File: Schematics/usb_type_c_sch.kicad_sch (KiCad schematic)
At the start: 4 parts, among them J2 USB_C_Receptacle

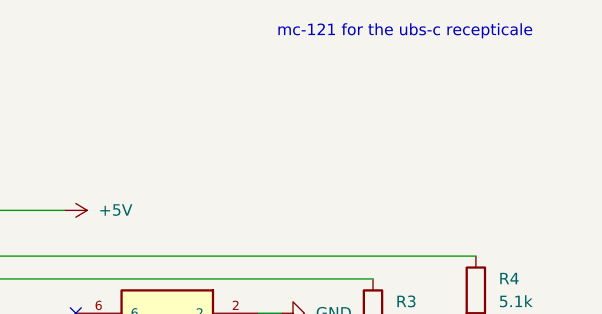
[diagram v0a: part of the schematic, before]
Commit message: finished sensor schematics, added datasheets organized files
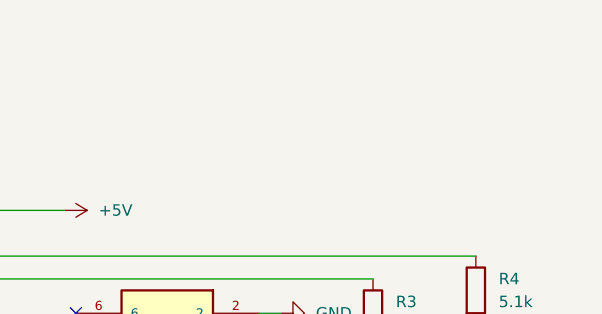
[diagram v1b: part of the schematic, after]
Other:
- note removed: "mc-121 for the ubs-c recepticale"
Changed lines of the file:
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@@
 	(generator_version "9.0")
 	(paper "A4")
-	(text "\n"
-		(exclude_from_sim no)
-		(at 157.226 37.338 0)
-		(effects
-			(font
-				(size 1.27 1.27)
-			)
-		)
-	)
-	(text "mc-121 for the ubs-c recepticale\n"
-		(exclude_from_sim no)
-		(at 178.816 37.338 0)
-		(effects
-			(font
-				(size 1.27 1.27)
-			)
-		)
-	)
 	(junction
 		(at 129.54 71.12)

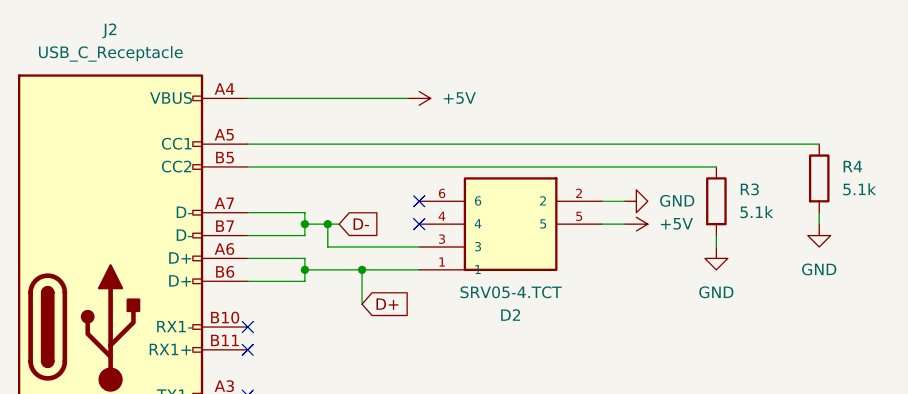
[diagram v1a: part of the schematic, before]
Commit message: added LCSC numbers and footprint values, need to connect schemeatic pins, then can start layout
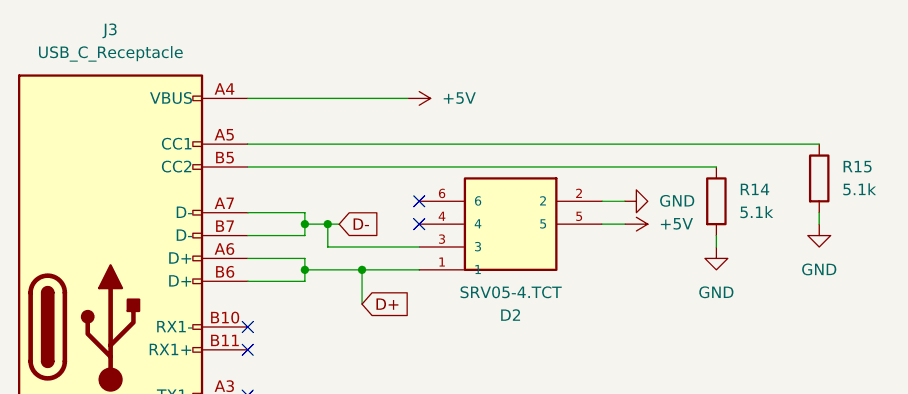
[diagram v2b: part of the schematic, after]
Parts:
- D2: footprint Library:SOT95P280X145-6N -> myFootprints:SOT95P280X145-6N; LCSC Part (none) -> C13612
- J3: renamed from J2; LCSC Part (none) -> C49566391
- R14: renamed from R3; LCSC Part (none) -> C27834
- R15: renamed from R4; LCSC Part (none) -> C27834
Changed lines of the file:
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@@
 		(dnp no)
 		(fields_autoplaced yes)
-		(property "Reference" "J2"
+		(property "Reference" "J3"
 			(at 107.95 49.53 0)
 			(effects
@@
 		)
 		(property "Description" "USB Full-Featured Type-C Receptacle connector"
+			(at 107.95 82.55 0)
+			(effects
+				(font
+					(size 1.27 1.27)
+				)
+				(hide yes)
+			)
+		)
+		(property "Sim.Device" ""
+			(at 107.95 82.55 0)
+			(effects
+				(font
+					(size 1.27 1.27)
+				)
+				(hide yes)
+			)
+		)
+		(property "Sim.Type" ""
+			(at 107.95 82.55 0)
+			(effects
+				(font
+					(size 1.27 1.27)
+				)
+				(hide yes)
+			)
+		)
+		(property "LCSC Part" "C49566391"
 			(at 107.95 82.55 0)
 			(effects
@@
 			(project "flightcomputer2"
 				(path "/6cb3dda3-5fe8-4715-b831-354360aa3199/105f27ec-5fab-44f4-a683-69b23a7486f0"
-					(reference "J2")
+					(reference "J3")
 					(unit 1)
 				)
@@
 			)
 		)
-		(property "Footprint" "Library:SOT95P280X145-6N"
+		(property "Footprint" "myFootprints:SOT95P280X145-6N"
 			(at 162.56 73.66 0)
 			(effects
@@
 				)
 				(justify bottom)
+				(hide yes)
+			)
+		)
+		(property "Sim.Device" ""
+			(at 162.56 73.66 0)
+			(effects
+				(font
+					(size 1.27 1.27)
+				)
+				(hide yes)
+			)
+		)
+		(property "Sim.Type" ""
+			(at 162.56 73.66 0)
+			(effects
+				(font
+					(size 1.27 1.27)
+				)
+				(hide yes)
+			)
+		)
+		(property "LCSC Part" "C13612"
+			(at 162.56 73.66 0)
+			(effects
+				(font
+					(size 1.27 1.27)
+				)
 				(hide yes)
 			)
@@
 		(on_board yes)
 		(dnp no)
-		(property "Reference" "#PWR052"
+		(property "Reference" "#PWR048"
 			(at 161.29 71.12 0)
 			(effects
@@
 			(project "flightcomputer2"
 				(path "/6cb3dda3-5fe8-4715-b831-354360aa3199/105f27ec-5fab-44f4-a683-69b23a7486f0"
-					(reference "#PWR052")
+					(reference "#PWR048")
 					(unit 1)
 				)
@@
 		(dnp no)
 		(fields_autoplaced yes)
-		(property "Reference" "#PWR050"
+		(property "Reference" "#PWR045"
 			(at 137.16 57.15 0)
 			(effects
@@
 			(project "flightcomputer2"
 				(path "/6cb3dda3-5fe8-4715-b831-354360aa3199/105f27ec-5fab-44f4-a683-69b23a7486f0"
-					(reference "#PWR050")
+					(reference "#PWR045")
 					(unit 1)
 				)
@@
 		(dnp no)
 		(fields_autoplaced yes)
-		(property "Reference" "R4"
+		(property "Reference" "R15"
 			(at 189.23 64.7699 0)
 			(effects
@@
 		)
 		(property "Description" "Resistor"
+			(at 186.69 66.04 0)
+			(effects
+				(font
+					(size 1.27 1.27)
+				)
+				(hide yes)
+			)
+		)
+		(property "Sim.Device" ""
+			(at 186.69 66.04 0)
+			(effects
+				(font
+					(size 1.27 1.27)
+				)
+				(hide yes)
+			)
+		)
+		(property "Sim.Type" ""
+			(at 186.69 66.04 0)
+			(effects
+				(font
+					(size 1.27 1.27)
+				)
+				(hide yes)
+			)
+		)
+		(property "LCSC Part" "C27834"
 			(at 186.69 66.04 0)
 			(effects
@@
 			(project "flightcomputer2"
 				(path "/6cb3dda3-5fe8-4715-b831-354360aa3199/105f27ec-5fab-44f4-a683-69b23a7486f0"
-					(reference "R4")
+					(reference "R15")
 					(unit 1)
 				)
@@
 		(dnp no)
 		(fields_autoplaced yes)
-		(property "Reference" "#PWR048"
+		(property "Reference" "#PWR051"
 			(at 175.26 80.01 0)
 			(effects
@@
 			(project "flightcomputer2"
 				(path "/6cb3dda3-5fe8-4715-b831-354360aa3199/105f27ec-5fab-44f4-a683-69b23a7486f0"
-					(reference "#PWR048")
+					(reference "#PWR051")
 					(unit 1)
 				)
@@
 		(on_board yes)
 		(dnp no)
-		(property "Reference" "#PWR051"
+		(property "Reference" "#PWR047"
 			(at 171.45 68.58 0)
 			(effects
@@
 			(project "flightcomputer2"
 				(path "/6cb3dda3-5fe8-4715-b831-354360aa3199/105f27ec-5fab-44f4-a683-69b23a7486f0"
-					(reference "#PWR051")
+					(reference "#PWR047")
 					(unit 1)
 				)
@@
 		(dnp no)
 		(fields_autoplaced yes)
-		(property "Reference" "#PWR047"
+		(property "Reference" "#PWR043"
 			(at 104.14 134.62 0)
 			(effects
@@
 			(project "flightcomputer2"
 				(path "/6cb3dda3-5fe8-4715-b831-354360aa3199/105f27ec-5fab-44f4-a683-69b23a7486f0"
-					(reference "#PWR047")
+					(reference "#PWR043")
 					(unit 1)
 				)
@@
 		(dnp no)
 		(fields_autoplaced yes)
-		(property "Reference" "R3"
+		(property "Reference" "R14"
 			(at 177.8 67.3099 0)
 			(effects
@@
 		)
 		(property "Description" "Resistor"
+			(at 175.26 68.58 0)
+			(effects
+				(font
+					(size 1.27 1.27)
+				)
+				(hide yes)
+			)
+		)
+		(property "Sim.Device" ""
+			(at 175.26 68.58 0)
+			(effects
+				(font
+					(size 1.27 1.27)
+				)
+				(hide yes)
+			)
+		)
+		(property "Sim.Type" ""
+			(at 175.26 68.58 0)
+			(effects
+				(font
+					(size 1.27 1.27)
+				)
+				(hide yes)
+			)
+		)
+		(property "LCSC Part" "C27834"
 			(at 175.26 68.58 0)
 			(effects
@@
 			(project "flightcomputer2"
 				(path "/6cb3dda3-5fe8-4715-b831-354360aa3199/105f27ec-5fab-44f4-a683-69b23a7486f0"
-					(reference "R3")
+					(reference "R14")
 					(unit 1)
 				)
@@
 		(dnp no)
 		(fields_autoplaced yes)
-		(property "Reference" "#PWR049"
+		(property "Reference" "#PWR052"
 			(at 186.69 77.47 0)
 			(effects
@@
 			(project "flightcomputer2"
 				(path "/6cb3dda3-5fe8-4715-b831-354360aa3199/105f27ec-5fab-44f4-a683-69b23a7486f0"
-					(reference "#PWR049")
+					(reference "#PWR052")
 					(unit 1)
 				)

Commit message: started lora schematic all pcb parts should be included
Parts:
- D2: DESCRIPTION Semtech SRV05-4.TCT, Uni-Directional TVS Diode Array, 300W,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 -> (none); Description_1 ESD Suppressors / TVS Diodes SOT-23 5V 4DIODE Low Capacitan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 -> (none); MF UMW -> (none); MOUSER_PART_NUMBER 947-SRV05-4.TCT -> (none); MOUSER_PRICE-STOCK https://www.mouser.com/Search/Refine.aspx?Keyword=947-SRV05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 -> (none); MP SRV05-4.TCT -> (none); Package None -> (none); Price None -> (none)
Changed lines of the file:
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@@
-			)
-		)
-		(property "Sim.Device" ""
-			(at 107.95 82.55 0)
-			(effects
-				(font
-					(size 1.27 1.27)
-				)
-				(hide yes)
-			)
-		)
-		(property "Sim.Type" ""
-			(at 107.95 82.55 0)
-			(effects
-				(font
-					(size 1.27 1.27)
-				)
-				(hide yes)
 			)
 		)
@@
 			)
 		)
-		(property "MF" "UMW"
+		(property "Check_prices" "https://www.snapeda.com/parts/SRV05-4.TCT/UMW/view-part/?ref=eda"
 			(at 162.56 73.66 0)
 			(effects
@@
 			)
 		)
-		(property "MOUSER_PRICE-STOCK" "https://www.mouser.com/Search/Refine.aspx?Keyword=947-SRV05-4.TCT"
+		(property "HEIGHT" "1.45mm"
 			(at 162.56 73.66 0)
 			(effects
@@
 			)
 		)
-		(property "DESCRIPTION" "Semtech SRV05-4.TCT, Uni-Directional TVS Diode Array, 300W, 6-Pin SOT-23"
+		(property "SnapEDA_Link" "https://www.snapeda.com/parts/SRV05-4.TCT/UMW/view-part/?ref=snap"
 			(at 162.56 73.66 0)
 			(effects
@@
 			)
 		)
-		(property "MOUSER_PART_NUMBER" "947-SRV05-4.TCT"
+		(property "Availability" "In Stock"
 			(at 162.56 73.66 0)
 			(effects
@@
 			)
 		)
-		(property "Price" "None"
+		(property "MANUFACTURER_PART_NUMBER" "SRV05-4.TCT"
 			(at 162.56 73.66 0)
 			(effects
@@
 				)
 				(justify bottom)
-				(hide yes)
-			)
-		)
-		(property "Package" "None"
-			(at 162.56 73.66 0)
-			(effects
-				(font
-					(size 1.27 1.27)
-				)
-				(justify bottom)
-				(hide yes)
-			)
-		)
-		(property "Check_prices" "https://www.snapeda.com/parts/SRV05-4.TCT/UMW/view-part/?ref=eda"
-			(at 162.56 73.66 0)
-			(effects
-				(font
-					(size 1.27 1.27)
-				)
-				(justify bottom)
-				(hide yes)
-			)
-		)
-		(property "HEIGHT" "1.45mm"
-			(at 162.56 73.66 0)
-			(effects
-				(font
-					(size 1.27 1.27)
-				)
-				(justify bottom)
-				(hide yes)
-			)
-		)
-		(property "SnapEDA_Link" "https://www.snapeda.com/parts/SRV05-4.TCT/UMW/view-part/?ref=snap"
-			(at 162.56 73.66 0)
-			(effects
-				(font
-					(size 1.27 1.27)
-				)
-				(justify bottom)
-				(hide yes)
-			)
-		)
-		(property "MP" "SRV05-4.TCT"
-			(at 162.56 73.66 0)
-			(effects
-				(font
-					(size 1.27 1.27)
-				)
-				(justify bottom)
-				(hide yes)
-			)
-		)
-		(property "Description_1" "ESD Suppressors / TVS Diodes SOT-23 5V 4DIODE Low Capacitance"
-			(at 162.56 73.66 0)
-			(effects
-				(font
-					(size 1.27 1.27)
-				)
-				(justify bottom)
-				(hide yes)
-			)
-		)
-		(property "Availability" "In Stock"
-			(at 162.56 73.66 0)
-			(effects
-				(font
-					(size 1.27 1.27)
-				)
-				(justify bottom)
-				(hide yes)
-			)
-		)
-		(property "MANUFACTURER_PART_NUMBER" "SRV05-4.TCT"
-			(at 162.56 73.66 0)
-			(effects
-				(font
-					(size 1.27 1.27)
-				)
-				(justify bottom)
-				(hide yes)
-			)
-		)
-		(property "Sim.Device" ""
-			(at 162.56 73.66 0)
-			(effects
-				(font
-					(size 1.27 1.27)
-				)
-				(hide yes)
-			)
-		)
-		(property "Sim.Type" ""
-			(at 162.56 73.66 0)
-			(effects
-				(font
-					(size 1.27 1.27)
-				)
 				(hide yes)
 			)
@@
 			)
 		)
-		(property "Sim.Device" ""
-			(at 186.69 66.04 0)
-			(effects
-				(font
-					(size 1.27 1.27)
-				)
-				(hide yes)
-			)
-		)
-		(property "Sim.Type" ""
-			(at 186.69 66.04 0)
-			(effects
-				(font
-					(size 1.27 1.27)
-				)
-				(hide yes)
-			)
-		)
 		(property "LCSC Part" "C27834"
 			(at 186.69 66.04 0)
@@
 			(at 175.26 68.58 0)
 			(effects
-				(font
-					(size 1.27 1.27)
-				)
-				(hide yes)
-			)
-		)
-		(property "Sim.Device" ""
-			(at 175.26 68.58 0)
-			(effects
-				(font
-					(size 1.27 1.27)
-				)
-				(hide yes)
-			)
-		)
-		(property "Sim.Type" ""
-			(at 175.26 68.58 0)
-			(effects

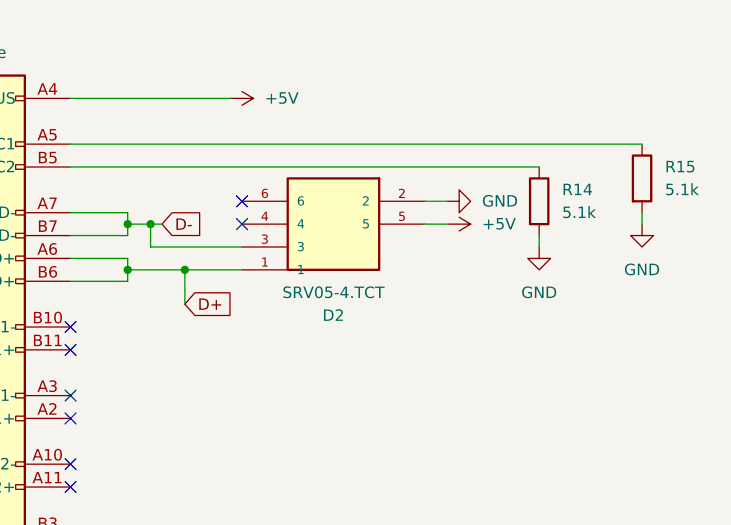
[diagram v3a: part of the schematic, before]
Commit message: added lora correct and organizing sheet pins
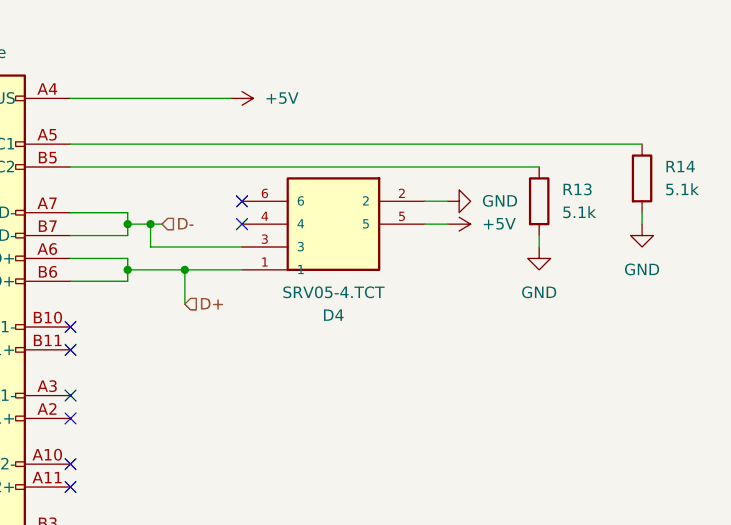
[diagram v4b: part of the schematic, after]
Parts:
- renumbered D2 to D4, R14 to R13, R15 to R14
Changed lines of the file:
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@@
 		)
 	)
-	(global_label "D-"
+	(hierarchical_label "D-"
 		(shape input)
 		(at 133.35 71.12 0)
-		(fields_autoplaced yes)
 		(effects
 			(font
@@
 			(justify left)
 		)
-		(property "Intersheetrefs" "${INTERSHEET_REFS}"
-			(at 139.1776 71.12 0)
-			(effects
-				(font
-					(size 1.27 1.27)
-				)
-				(justify left)
-				(hide yes)
-			)
-		)
-	)
-	(global_label "D+"
+	)
+	(hierarchical_label "D+"
 		(shape input)
 		(at 135.89 80.01 0)
-		(fields_autoplaced yes)
 		(effects
 			(font
@@
 			(justify left)
 		)
-		(property "Intersheetrefs" "${INTERSHEET_REFS}"
-			(at 141.7176 80.01 0)
-			(effects
-				(font
-					(size 1.27 1.27)
-				)
-				(justify left)
-				(hide yes)
-			)
-		)
 	)
 	(symbol
@@
 		(dnp no)
 		(fields_autoplaced yes)
-		(property "Reference" "D2"
+		(property "Reference" "D4"
 			(at 152.4 81.28 0)
 			(effects
@@
 			(project "flightcomputer2"
 				(path "/6cb3dda3-5fe8-4715-b831-354360aa3199/105f27ec-5fab-44f4-a683-69b23a7486f0"
-					(reference "D2")
+					(reference "D4")
 					(unit 1)
 				)
@@
 		(on_board yes)
 		(dnp no)
-		(property "Reference" "#PWR048"
+		(property "Reference" "#PWR051"
 			(at 161.29 71.12 0)
 			(effects
@@
 			(project "flightcomputer2"
 				(path "/6cb3dda3-5fe8-4715-b831-354360aa3199/105f27ec-5fab-44f4-a683-69b23a7486f0"
-					(reference "#PWR048")
+					(reference "#PWR051")
 					(unit 1)
 				)
@@
 		(dnp no)
 		(fields_autoplaced yes)
-		(property "Reference" "#PWR045"
+		(property "Reference" "#PWR048"
 			(at 137.16 57.15 0)
 			(effects
@@
 			(project "flightcomputer2"
 				(path "/6cb3dda3-5fe8-4715-b831-354360aa3199/105f27ec-5fab-44f4-a683-69b23a7486f0"
-					(reference "#PWR045")
+					(reference "#PWR048")
 					(unit 1)
 				)
@@
 		(dnp no)
 		(fields_autoplaced yes)
-		(property "Reference" "R15"
+		(property "Reference" "R14"
 			(at 189.23 64.7699 0)
 			(effects
@@
 			(project "flightcomputer2"
 				(path "/6cb3dda3-5fe8-4715-b831-354360aa3199/105f27ec-5fab-44f4-a683-69b23a7486f0"
-					(reference "R15")
+					(reference "R14")
 					(unit 1)
 				)
@@
 		(dnp no)
 		(fields_autoplaced yes)
-		(property "Reference" "#PWR051"
+		(property "Reference" "#PWR052"
 			(at 175.26 80.01 0)
 			(effects
@@
 			(project "flightcomputer2"
 				(path "/6cb3dda3-5fe8-4715-b831-354360aa3199/105f27ec-5fab-44f4-a683-69b23a7486f0"
-					(reference "#PWR051")
+					(reference "#PWR052")
 					(unit 1)
 				)
@@
 		(on_board yes)
 		(dnp no)
-		(property "Reference" "#PWR047"
+		(property "Reference" "#PWR050"
 			(at 171.45 68.58 0)
 			(effects
@@
 			(project "flightcomputer2"
 				(path "/6cb3dda3-5fe8-4715-b831-354360aa3199/105f27ec-5fab-44f4-a683-69b23a7486f0"
-					(reference "#PWR047")
+					(reference "#PWR050")
 					(unit 1)
 				)
@@
 		(dnp no)
 		(fields_autoplaced yes)
-		(property "Reference" "#PWR043"
+		(property "Reference" "#PWR045"
 			(at 104.14 134.62 0)
 			(effects
@@
 			(project "flightcomputer2"
 				(path "/6cb3dda3-5fe8-4715-b831-354360aa3199/105f27ec-5fab-44f4-a683-69b23a7486f0"
-					(reference "#PWR043")
+					(reference "#PWR045")
 					(unit 1)
 				)
@@
 		(dnp no)
 		(fields_autoplaced yes)
-		(property "Reference" "R14"
+		(property "Reference" "R13"
 			(at 177.8 67.3099 0)
 			(effects
@@
 			(project "flightcomputer2"
 				(path "/6cb3dda3-5fe8-4715-b831-354360aa3199/105f27ec-5fab-44f4-a683-69b23a7486f0"
-					(reference "R14")
+					(reference "R13")
 					(unit 1)
 				)
@@
 		(dnp no)
 		(fields_autoplaced yes)
-		(property "Reference" "#PWR052"
+		(property "Reference" "#PWR053"
 			(at 186.69 77.47 0)
 			(effects
@@
 			(project "flightcomputer2"
 				(path "/6cb3dda3-5fe8-4715-b831-354360aa3199/105f27ec-5fab-44f4-a683-69b23a7486f0"
-					(reference "#PWR052")
-					(unit 1)
-				)
+					(reference "#PWR053")
+					(unit 1)
+				)
